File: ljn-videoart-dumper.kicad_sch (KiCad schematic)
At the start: 5 parts, among them J1 Power, J2 Digital/PWM, J3 Analog, J4 Digital/PWM, J5 Video Art Edge

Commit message: Add connector
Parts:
- J5: footprint (none) -> TE_AMP_5530843-3:CONN_5530843-3_TYC
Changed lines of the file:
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@@
       (effects (font (size 1.27 1.27)))
     )
-    (property "Footprint" "" (at 125.095 97.155 0)
+    (property "Footprint" "TE_AMP_5530843-3:CONN_5530843-3_TYC" (at 125.095 97.155 0)
       (effects (font (size 1.27 1.27)) hide)
     )

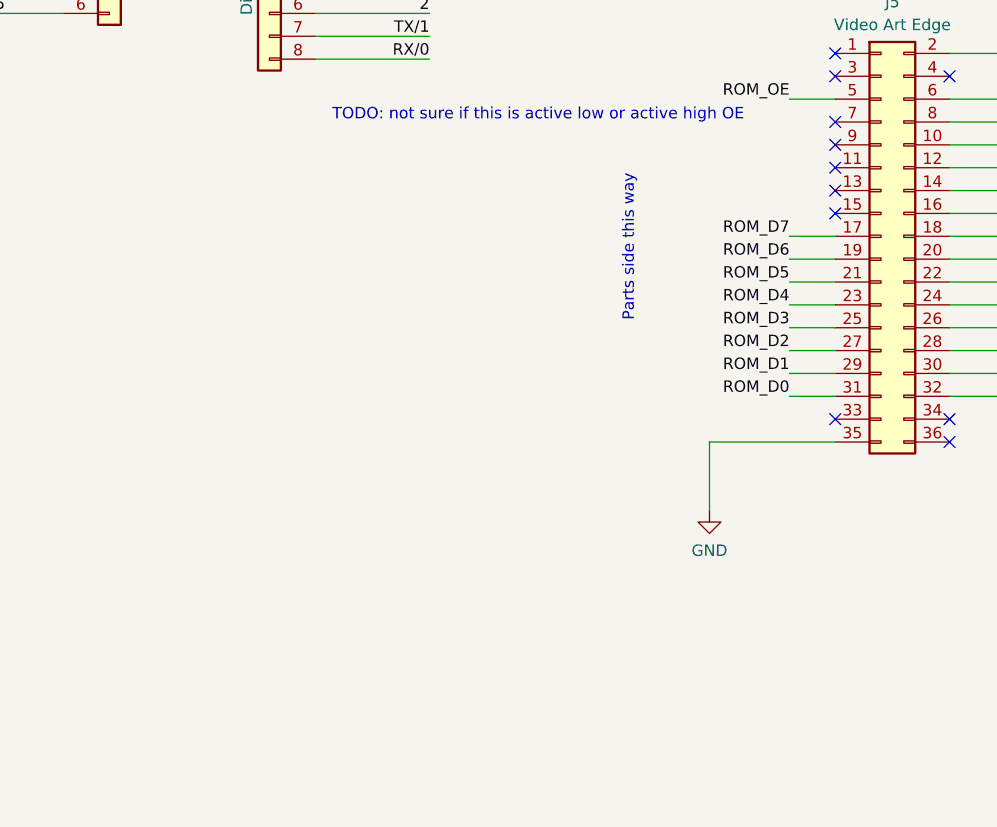
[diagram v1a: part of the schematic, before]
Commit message: Fix pin numbering before it gets embarrassing
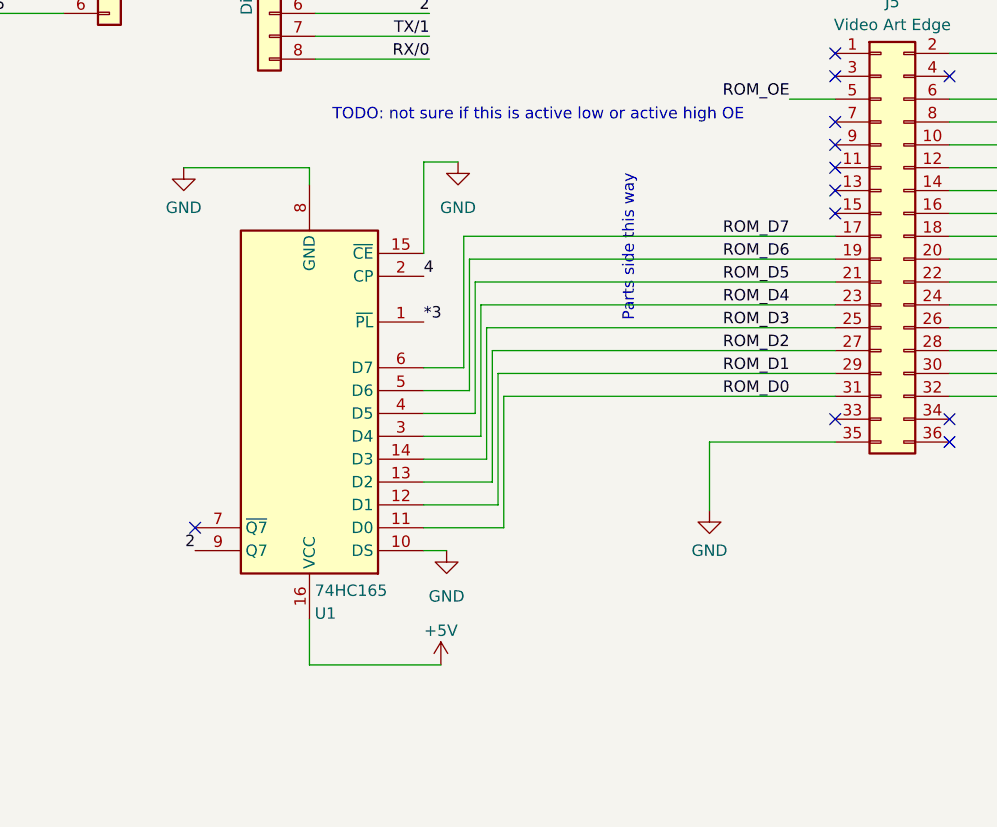
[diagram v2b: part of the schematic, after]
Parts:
- added U1: 74HC165, Package_DIP:DIP-16_W7.62mm_Socket_LongPads, symbol 74xx:74HC165
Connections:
- net *3: now also U1.1 (~{PL})
- net +5V: now also U1.16 (VCC)
- net 2: now also U1.9 (Q7)
- net 4: now also U1.2 (CP)
- net GND: now also U1.10 (DS), U1.15 (~{CE}), U1.8 (GND)
- net ROM_D0: now also U1.11 (D0)
- net ROM_D1: now also U1.12 (D1)
- net ROM_D2: now also U1.13 (D2)
- net ROM_D3: now also U1.14 (D3)
- net ROM_D4: now also U1.3 (D4)
- net ROM_D5: now also U1.4 (D5)
- net ROM_D6: now also U1.5 (D6)
- net ROM_D7: now also U1.6 (D7)
- no-connect marks 12 -> 13

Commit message: 595s
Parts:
- added U2, U3: 74HC595, Package_DIP:DIP-16_W7.62mm_Socket_LongPads, symbol 74xx:74HC595
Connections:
- net *11: now also U2.14 (SER)
- net +5V: now also U2.16 (VCC), U3.16 (VCC)
- net 12: now also U2.11 (SRCLK), U3.11 (SRCLK)
- net 8: now also U2.12 (RCLK), U3.12 (RCLK)
- net GND: now also U2.13 (~{OE}), U2.8 (GND), U3.13 (~{OE}), U3.8 (GND)
- new net: U2.9 (QH'), U3.14 (SER)
- no-connect marks 13 -> 16
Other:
- note added: "TODO: Connect to ROM"
- note added: "What's the bit order on the 595 if I just want to send a straight address out of the arduino?"

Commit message: Final re-route
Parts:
- added R1: 0Ω, Resistor_THT:R_Axial_DIN0207_L6.3mm_D2.5mm_P10.16mm_Horizontal, symbol Device:R_Small_US
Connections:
- net *10: now also R1.1
- net ROM_A0: now also U2.15 (QA)
- net ROM_A1: now also U2.1 (QB)
- net ROM_A10: now also U3.2 (QC)
- net ROM_A11: now also U3.3 (QD)
- net ROM_A12: now also U3.4 (QE)
- net ROM_A13: now also U3.5 (QF)
- net ROM_A2: now also U2.2 (QC)
- net ROM_A3: now also U2.3 (QD)
- net ROM_A4: now also U2.4 (QE)
- net ROM_A5: now also U2.5 (QF)
- net ROM_A6: now also U2.6 (QG)
- net ROM_A7: now also U2.7 (QH)
- net ROM_A8: now also U3.15 (QA)
- net ROM_A9: now also U3.1 (QB)
- net ROM_OE: now also R1.2
- no-connect marks 16 -> 18
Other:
- note added: "TODO: Other, larger ROMs might use this as bank switching but we have no idea where they go, or even if those ROMs exist"
- note added: "remember to shift MSBFIRST"
- note removed: "TODO: Connect to ROM"
- note removed: "What's the bit order on the 595 if I just want to send a straight address out of the arduino?"
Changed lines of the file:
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@@
   (no_connect (at 132.715 120.015))
   (no_connect (at 48.895 129.54))
+  (no_connect (at 215.265 125.73))
   (no_connect (at 120.015 79.375))
   (no_connect (at 132.715 79.375))
@@
   (no_connect (at 120.015 76.835))
   (no_connect (at 120.015 86.995))
+  (no_connect (at 215.265 123.19))
   (no_connect (at 194.945 115.57))
   (no_connect (at 34.29 31.75))
@@
     (stroke (width 0) (type solid))
   )
-  (wire (pts (xy 62.23 44.45) (xy 74.93 44.45))
+  (wire (pts (xy 62.23 44.45) (xy 80.01 44.45))
     (stroke (width 0) (type solid))
   )
@@
     (stroke (width 0) (type solid))
   )
+  (wire (pts (xy 80.01 66.675) (xy 80.01 44.45))
+    (stroke (width 0) (type default))
+  )
   (wire (pts (xy 74.295 129.54) (xy 83.185 129.54))
     (stroke (width 0) (type default))
@@
     (stroke (width 0) (type default))
   )
+  (wire (pts (xy 95.885 66.675) (xy 80.01 66.675))
+    (stroke (width 0) (type default))
+  )
   (wire (pts (xy 132.715 84.455) (xy 139.7 84.455))
     (stroke (width 0) (type default))
@@
     (stroke (width 0) (type default))
   )
+  (wire (pts (xy 95.885 72.39) (xy 95.885 81.915))
+    (stroke (width 0) (type default))
+  )
   (wire (pts (xy 34.29 64.77) (xy 21.59 64.77))
     (stroke (width 0) (type solid))
@@
     (stroke (width 0) (type solid))
   )
-  (wire (pts (xy 114.935 81.915) (xy 120.015 81.915))
+  (wire (pts (xy 95.885 81.915) (xy 120.015 81.915))
     (stroke (width 0) (type default))
   )
@@
     (stroke (width 0) (type default))
   )
+  (wire (pts (xy 95.885 66.675) (xy 95.885 67.31))
+    (stroke (width 0) (type default))
+  )
   (wire (pts (xy 80.645 104.775) (xy 120.015 104.775))
     (stroke (width 0) (type default))
@@
     (stroke (width 0) (type solid))
   )
-  (text "TODO: Connect to ROM" (at 227.33 76.2 0)
-    (effects (font (size 1.27 1.27)) (justify left bottom))
-  )
-  (text "What's the bit order on the 595 if I just want to send a straight address out of the arduino?"
-    (at 168.91 91.44 0)
+  (text "remember to shift MSBFIRST" (at 227.33 76.2 0)
     (effects (font (size 1.27 1.27)) (justify left bottom))
   )
@@
   )
   (text "also need to keep the USB lines open for serial, but i don't think it interferes with any of these"
-    (at 79.375 55.245 0)
+    (at 84.455 52.705 0)
+    (effects (font (size 1.27 1.27)) (justify left bottom))
+  )
+  (text "TODO: Other, larger ROMs might use this as bank\nswitching but we have no idea where they go, or\neven if those ROMs exist"
+    (at 220.98 129.54 0)
     (effects (font (size 1.27 1.27)) (justify left bottom))
   )
@@
     (effects (font (size 1.27 1.27)) (justify right bottom))
   )
+  (label "ROM_A0" (at 215.9 50.165 0) (fields_autoplaced)
+    (effects (font (size 1.27 1.27)) (justify left bottom))
+  )
   (label "2" (at 74.93 72.39 180) (fields_autoplaced)
     (effects (font (size 1.27 1.27)) (justify right bottom))
@@
     (effects (font (size 1.27 1.27)) (justify left bottom))
   )
+  (label "ROM_A3" (at 215.9 57.785 0) (fields_autoplaced)
+    (effects (font (size 1.27 1.27)) (justify left bottom))
+  )
+  (label "ROM_A11" (at 215.265 115.57 0) (fields_autoplaced)
+    (effects (font (size 1.27 1.27)) (justify left bottom))
+  )
   (label "13" (at 74.93 36.83 180) (fields_autoplaced)
     (effects (font (size 1.27 1.27)) (justify right bottom))
   )
+  (label "ROM_A6" (at 215.9 65.405 0) (fields_autoplaced)
+    (effects (font (size 1.27 1.27)) (justify left bottom))
+  )
+  (label "ROM_A7" (at 215.9 67.945 0) (fields_autoplaced)
+    (effects (font (size 1.27 1.27)) (justify left bottom))
+  )
   (label "ROM_A11" (at 139.7 109.855 0) (fields_autoplaced)
     (effects (font (size 1.27 1.27)) (justify left bottom))
@@
     (effects (font (size 1.27 1.27)) (justify left bottom))
   )
+  (label "ROM_A1" (at 215.9 52.705 0) (fields_autoplaced)
+    (effects (font (size 1.27 1.27)) (justify left bottom))
+  )
   (label "ROM_A13" (at 139.7 114.935 0) (fields_autoplaced)
     (effects (font (size 1.27 1.27)) (justify left bottom))
@@
     (effects (font (size 1.27 1.27)) (justify right bottom))
   )
+  (label "ROM_A13" (at 215.265 120.65 0) (fields_autoplaced)
+    (effects (font (size 1.27 1.27)) (justify left bottom))
+  )
   (label "ROM_OE" (at 114.935 81.915 180) (fields_autoplaced)
     (effects (font (size 1.27 1.27)) (justify right bottom))
@@
     (effects (font (size 1.27 1.27)) (justify right bottom))
   )
+  (label "ROM_A9" (at 215.265 110.49 0) (fields_autoplaced)
+    (effects (font (size 1.27 1.27)) (justify left bottom))
+  )
   (label "ROM_A1" (at 139.7 84.455 0) (fields_autoplaced)
     (effects (font (size 1.27 1.27)) (justify left bottom))
@@
     (effects (font (size 1.27 1.27)) (justify right bottom))
   )
+  (label "ROM_A10" (at 215.265 113.03 0) (fields_autoplaced)
+    (effects (font (size 1.27 1.27)) (justify left bottom))
+  )
   (label "A1" (at 21.59 62.23 0) (fields_autoplaced)
     (effects (font (size 1.27 1.27)) (justify left bottom))
@@
     (effects (font (size 1.27 1.27)) (justify left bottom))
   )
+  (label "ROM_A12" (at 215.265 118.11 0) (fields_autoplaced)
+    (effects (font (size 1.27 1.27)) (justify left bottom))
+  )
   (label "A0" (at 21.59 59.69 0) (fields_autoplaced)
     (effects (font (size 1.27 1.27)) (justify left bottom))
@@
     (effects (font (size 1.27 1.27)) (justify right bottom))
   )
+  (label "ROM_A8" (at 215.265 107.95 0) (fields_autoplaced)
+    (effects (font (size 1.27 1.27)) (justify left bottom))
+  )
   (label "*11" (at 195.58 50.165 180) (fields_autoplaced)
     (effects (font (size 1.27 1.27)) (justify right bottom))
   )
+  (label "ROM_A4" (at 215.9 60.325 0) (fields_autoplaced)
+    (effects (font (size 1.27 1.27)) (justify left bottom))
+  )
   (label "Vin" (at 26.67 26.67 270) (fields_autoplaced)
     (effects (font (size 1.27 1.27)) (justify right bottom))
@@
     (effects (font (size 1.27 1.27)) (justify left bottom))
   )
+  (label "ROM_A2" (at 215.9 55.245 0) (fields_autoplaced)
+    (effects (font (size 1.27 1.27)) (justify left bottom))
+  )
   (label "ROM_A0" (at 139.7 81.915 0) (fields_autoplaced)
     (effects (font (size 1.27 1.27)) (justify left bottom))
@@
   (label "ROM_D4" (at 114.935 104.775 180) (fields_autoplaced)
     (effects (font (size 1.27 1.27)) (justify right bottom))
+  )
+  (label "ROM_A5" (at 215.9 62.865 0) (fields_autoplaced)
+    (effects (font (size 1.27 1.27)) (justify left bottom))
   )
   (symbol (lib_id "Connector_Generic:Conn_01x08") (at 39.37 39.37 0) (unit 1)
@@
         )
       )
+    )
+  )
+  (symbol (lib_id "Device:R_Small_US") (at 95.885 69.85 0) (unit 1)
+    (in_bom yes) (on_board yes) (dnp no) (fields_autoplaced)
+    (property "Reference" "R1" (at 97.79 69.215 0)
+      (effects (font (size 1.27 1.27)) (justify left))
+    )
+    (property "Value" "0Ω" (at 97.79 71.755 0)
+      (effects (font (size 1.27 1.27)) (justify left))
+    )
+    (property "Footprint" "Resistor_THT:R_Axial_DIN0207_L6.3mm_D2.5mm_P10.16mm_Horizontal" (at 95.885 69.85 0)
+      (effects (font (size 1.27 1.27)) hide)
+    )
+    (property "Datasheet" "~" (at 95.885 69.85 0)
+      (effects (font (size 1.27 1.27)) hide)
+    )
+    (pin "1")
+    (pin "2")
+    (instances
+      (project "ljn-videoart-dumper"
+        (path "/e63e39d7-6ac0-4ffd-8aa3-1841a4541b55"
+          (reference "R1") (unit 1)
+        )
+      )

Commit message: Nothing I'm doing with address pins seems to matter?
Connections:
- net ROM_OE renamed ~{ROM_OE}
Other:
- note removed: "14 digital IOs on Uno"
- note removed: "Need to be able to latch 8 bits of data? (PISO SR)"
- note removed: "Need ~{OE}, ~{CE} Need A0...A13 (14 pins right there)"
- note removed: "TODO: Footprint"
- note removed: "TODO: not sure if this is active low or active high OE"
- note removed: "also need to keep the USB lines open for serial, but i don't think it interferes with any of these"
- note removed: "potentially other pins depending on how wonky the card edge is"
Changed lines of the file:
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@@
-    (effects (font (size 1.27 1.27)) (justify left bottom))
-  )
-  (text "potentially other pins depending on how wonky the card edge is"
-    (at 84.455 50.165 0)
-    (effects (font (size 1.27 1.27)) (justify left bottom))
-  )
-  (text "TODO: not sure if this is active low or active high OE"
-    (at 64.135 84.455 0)
-    (effects (font (size 1.27 1.27)) (justify left bottom))
-  )
-  (text "also need to keep the USB lines open for serial, but i don't think it interferes with any of these"
-    (at 84.455 52.705 0)
     (effects (font (size 1.27 1.27)) (justify left bottom))
   )
@@
     (effects (font (size 1.27 1.27)) (justify left bottom))
   )
-  (text "14 digital IOs on Uno" (at 97.155 33.02 0)
-    (effects (font (size 1.27 1.27)) (justify left bottom))
-  )
   (text "* Indicates a PWM-capable pin" (at 177.8 180.34 0)
     (effects (font (size 1.27 1.27)) (justify left bottom))
   )
-  (text "TODO: Footprint" (at 113.665 64.77 0)
-    (effects (font (size 1.27 1.27)) (justify left bottom))
-  )
-  (text "Need to be able to latch 8 bits of data? (PISO SR)"
-    (at 85.09 36.195 0)
-    (effects (font (size 1.27 1.27)) (justify left bottom))
-  )
   (text "Parts side this way" (at 97.79 106.68 90)
-    (effects (font (size 1.27 1.27)) (justify left bottom))
-  )
-  (text "Need ~{OE}, ~{CE}\nNeed A0...A13 (14 pins right there)"
-    (at 88.265 45.085 0)
     (effects (font (size 1.27 1.27)) (justify left bottom))
   )
@@
     (effects (font (size 1.27 1.27)) (justify left bottom))
   )
-  (label "ROM_OE" (at 114.935 81.915 180) (fields_autoplaced)
+  (label "~{ROM_OE}" (at 114.935 81.915 180) (fields_autoplaced)
     (effects (font (size 1.27 1.27)) (justify right bottom))
   )

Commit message: Fix errors, add 5v/gnd test points
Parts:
- added TP1: 5v, TestPoint:TestPoint_Loop_D2.54mm_Drill1.5mm_Beaded, symbol Connector:TestPoint
- added TP2: ground, TestPoint:TestPoint_Loop_D2.54mm_Drill1.5mm_Beaded, symbol Connector:TestPoint
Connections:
- net +5V: now also TP1.1
- net GND: now also TP2.1
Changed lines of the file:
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@@
+    (stroke (width 0) (type default))
+  )
+  (wire (pts (xy 107.315 33.02) (xy 116.205 33.02))
     (stroke (width 0) (type default))
   )
@@
     (stroke (width 0) (type default))
   )
+  (wire (pts (xy 116.205 33.02) (xy 116.205 30.48))
+    (stroke (width 0) (type default))
+  )
   (wire (pts (xy 61.595 89.535) (xy 61.595 91.44))
     (stroke (width 0) (type default))
@@
     (stroke (width 0) (type default))
   )
+  (wire (pts (xy 107.315 27.305) (xy 107.315 33.02))
+    (stroke (width 0) (type default))
+  )
   (wire (pts (xy 81.28 107.315) (xy 120.015 107.315))
     (stroke (width 0) (type default))
@@
   )
   (wire (pts (xy 80.01 102.235) (xy 120.015 102.235))
+    (stroke (width 0) (type default))
+  )
+  (wire (pts (xy 126.365 30.48) (xy 126.365 33.02))
     (stroke (width 0) (type default))
   )
@@
     )
   )
+  (symbol (lib_name "+5V_5") (lib_id "power:+5V") (at 107.315 27.305 0) (unit 1)
+    (in_bom yes) (on_board yes) (dnp no) (fields_autoplaced)
+    (property "Reference" "#PWR018" (at 107.315 31.115 0)
+      (effects (font (size 1.27 1.27)) hide)
+    )
+    (property "Value" "+5V" (at 107.315 22.86 0)
+      (effects (font (size 1.27 1.27)))
+    )
+    (property "Footprint" "" (at 107.315 27.305 0)
+      (effects (font (size 1.27 1.27)) hide)
+    )
+    (property "Datasheet" "" (at 107.315 27.305 0)
+      (effects (font (size 1.27 1.27)) hide)
+    )
+    (pin "1")
+    (instances
+      (project "ljn-videoart-dumper"
+        (path "/e63e39d7-6ac0-4ffd-8aa3-1841a4541b55"
+          (reference "#PWR018") (unit 1)
+        )
+      )
+    )
+  )
   (symbol (lib_name "+5V_2") (lib_id "power:+5V") (at 76.2 144.78 0) (unit 1)
     (in_bom yes) (on_board yes) (dnp no) (fields_autoplaced)
@@
         (path "/e63e39d7-6ac0-4ffd-8aa3-1841a4541b55"
           (reference "#PWR01") (unit 1)
+        )
+      )
+    )
+  )
+  (symbol (lib_name "GND_9") (lib_id "power:GND") (at 126.365 33.02 0) (unit 1)
+    (in_bom yes) (on_board yes) (dnp no) (fields_autoplaced)
+    (property "Reference" "#PWR019" (at 126.365 39.37 0)
+      (effects (font (size 1.27 1.27)) hide)
+    )
+    (property "Value" "GND" (at 126.365 38.1 0)
+      (effects (font (size 1.27 1.27)))
+    )
+    (property "Footprint" "" (at 126.365 33.02 0)
+      (effects (font (size 1.27 1.27)) hide)
+    )
+    (property "Datasheet" "" (at 126.365 33.02 0)
+      (effects (font (size 1.27 1.27)) hide)
+    )
+    (pin "1")
+    (instances
+      (project "ljn-videoart-dumper"
+        (path "/e63e39d7-6ac0-4ffd-8aa3-1841a4541b55"
+          (reference "#PWR019") (unit 1)
         )
       )
@@
     )
   )
+  (symbol (lib_id "Connector:TestPoint") (at 126.365 30.48 0) (unit 1)
+    (in_bom yes) (on_board yes) (dnp no) (fields_autoplaced)
+    (property "Reference" "TP2" (at 128.905 25.908 0)
+      (effects (font (size 1.27 1.27)) (justify left))
+    )
+    (property "Value" "ground" (at 128.905 28.448 0)
+      (effects (font (size 1.27 1.27)) (justify left))
+    )
+    (property "Footprint" "TestPoint:TestPoint_Loop_D2.54mm_Drill1.5mm_Beaded" (at 131.445 30.48 0)
+      (effects (font (size 1.27 1.27)) hide)
+    )
+    (property "Datasheet" "~" (at 131.445 30.48 0)
+      (effects (font (size 1.27 1.27)) hide)
+    )
+    (pin "1")
+    (instances
+      (project "ljn-videoart-dumper"
+        (path "/e63e39d7-6ac0-4ffd-8aa3-1841a4541b55"
+          (reference "TP2") (unit 1)
+        )
+      )
+    )
+  )
   (symbol (lib_name "+5V_3") (lib_id "power:+5V") (at 205.74 36.195 0) (unit 1)
     (in_bom yes) (on_board yes) (dnp no) (fields_autoplaced)
@@
         )
       )
+    )
+  )
+  (symbol (lib_id "Connector:TestPoint") (at 116.205 30.48 0) (unit 1)
+    (in_bom yes) (on_board yes) (dnp no) (fields_autoplaced)
+    (property "Reference" "TP1" (at 118.11 25.908 0)
+      (effects (font (size 1.27 1.27)) (justify left))
+    )
+    (property "Value" "5v" (at 118.11 28.448 0)
+      (effects (font (size 1.27 1.27)) (justify left))
+    )
+    (property "Footprint" "TestPoint:TestPoint_Loop_D2.54mm_Drill1.5mm_Beaded" (at 121.285 30.48 0)
+      (effects (font (size 1.27 1.27)) hide)
+    )
+    (property "Datasheet" "~" (at 121.285 30.48 0)
+      (effects (font (size 1.27 1.27)) hide)
+    )
+    (pin "1")
+    (instances
+      (project "ljn-videoart-dumper"
+        (path "/e63e39d7-6ac0-4ffd-8aa3-1841a4541b55"
+          (reference "TP1") (unit 1)
+        )
+      )
